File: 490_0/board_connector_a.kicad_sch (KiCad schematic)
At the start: 7 parts, among them J21 DF40HC(3.0)-100DS-0.4V(58), J22 DF40HC(3.0)-100DS-0.4V(58), J23 TS-102-G-A

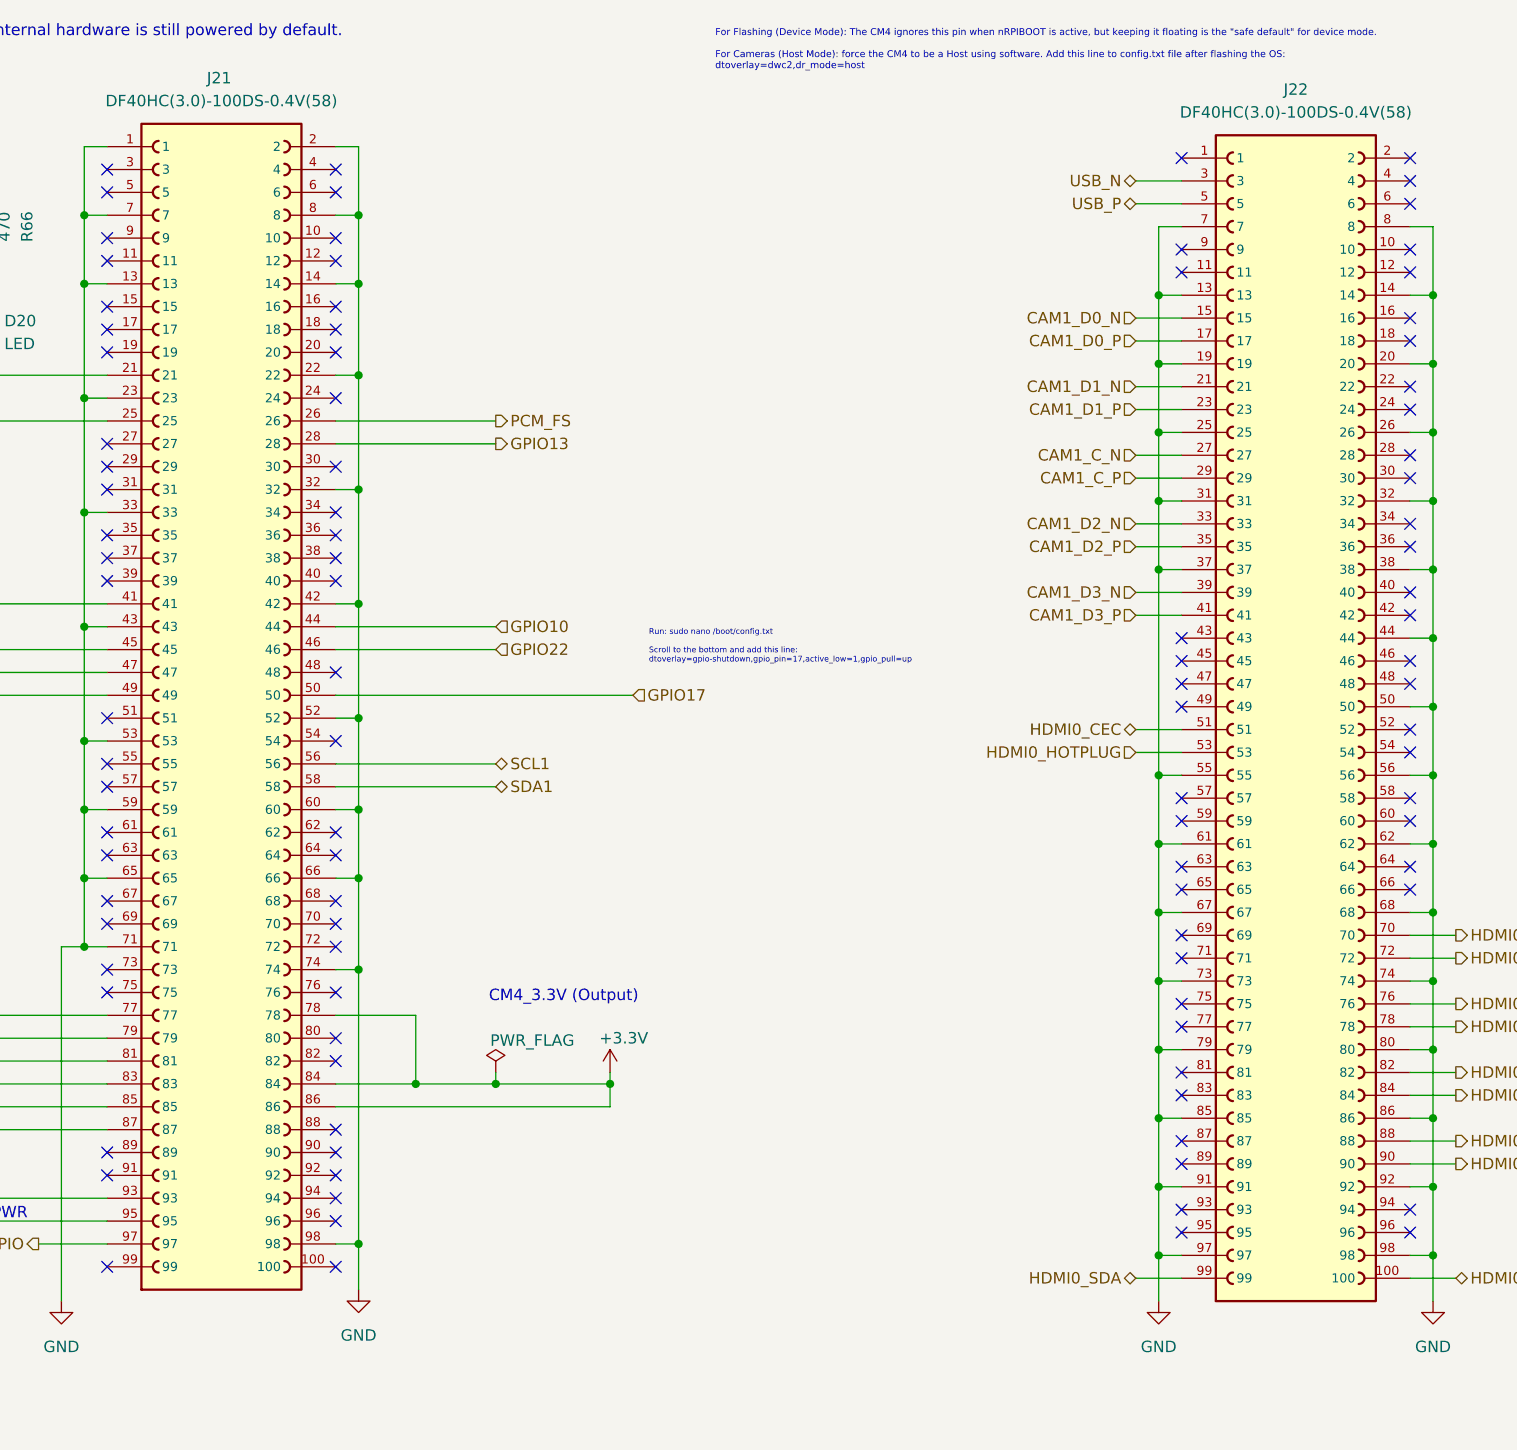
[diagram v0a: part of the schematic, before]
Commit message: Changed buck converter chip
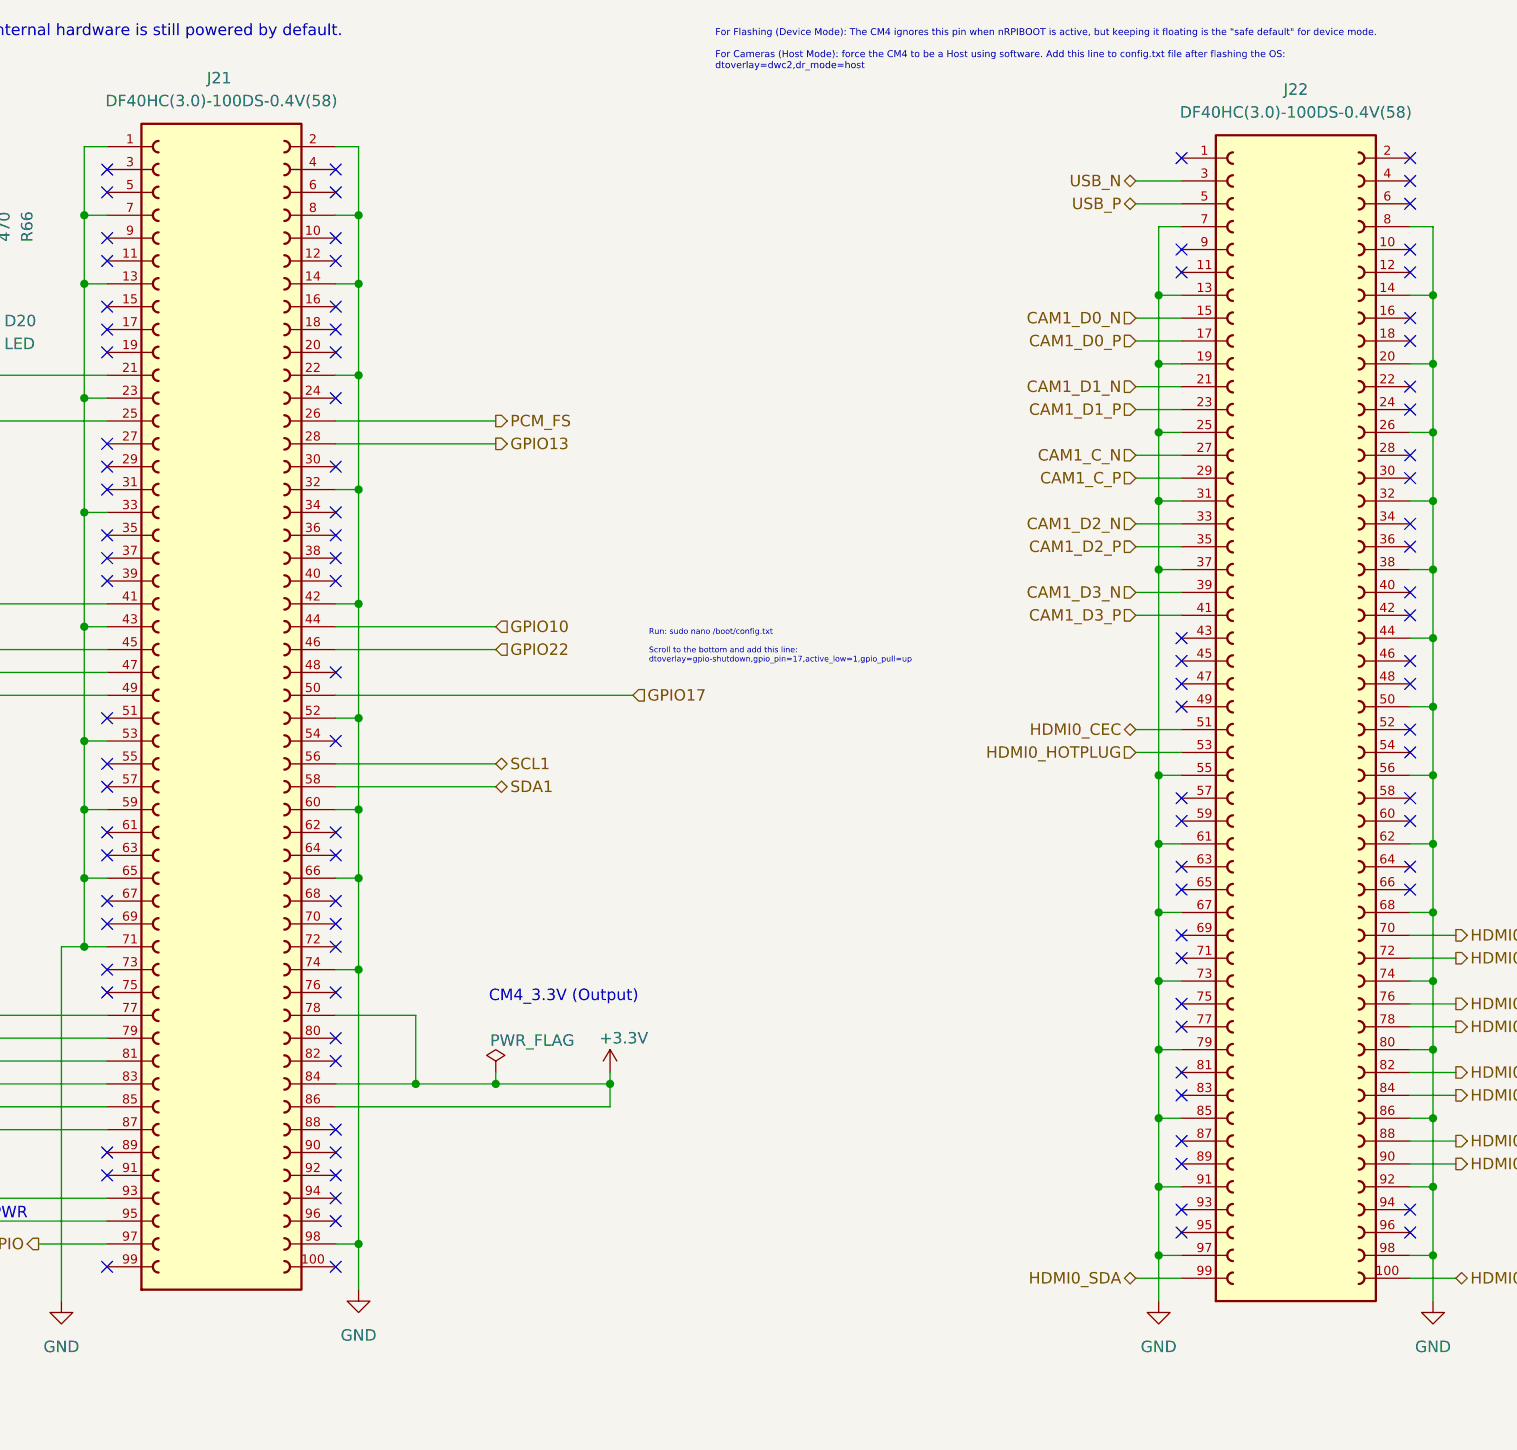
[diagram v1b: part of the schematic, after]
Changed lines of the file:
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@@
 	)
 	(symbol
+		(lib_name "DF40C-100DS-0.4V_51__1")
 		(lib_id "capstone_parts:DF40C-100DS-0.4V_51_")
 		(at 111.76 87.63 0)

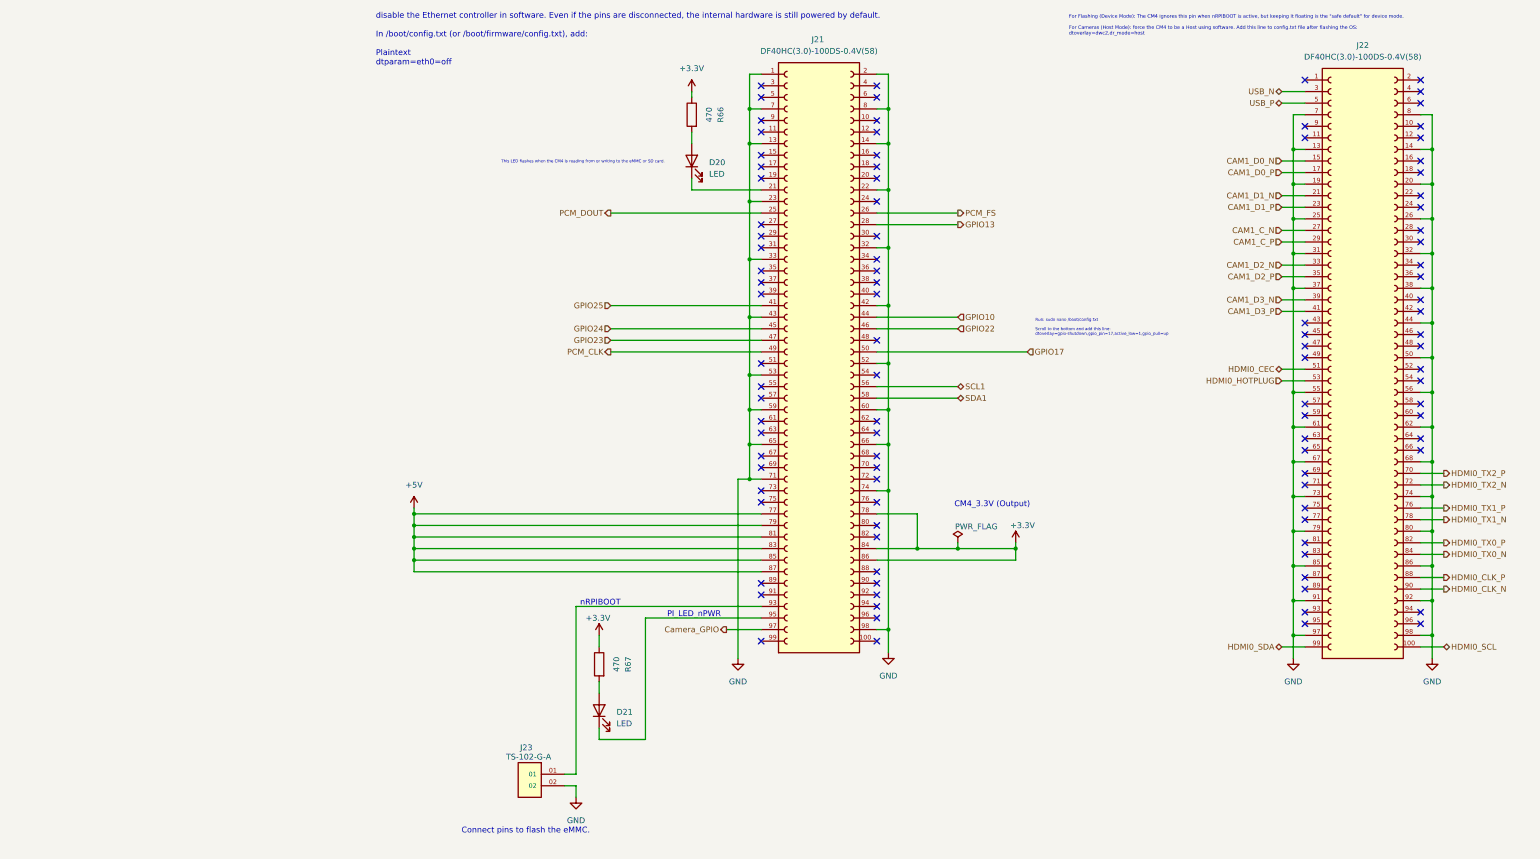
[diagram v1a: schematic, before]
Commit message: Implemented Dmitry comments
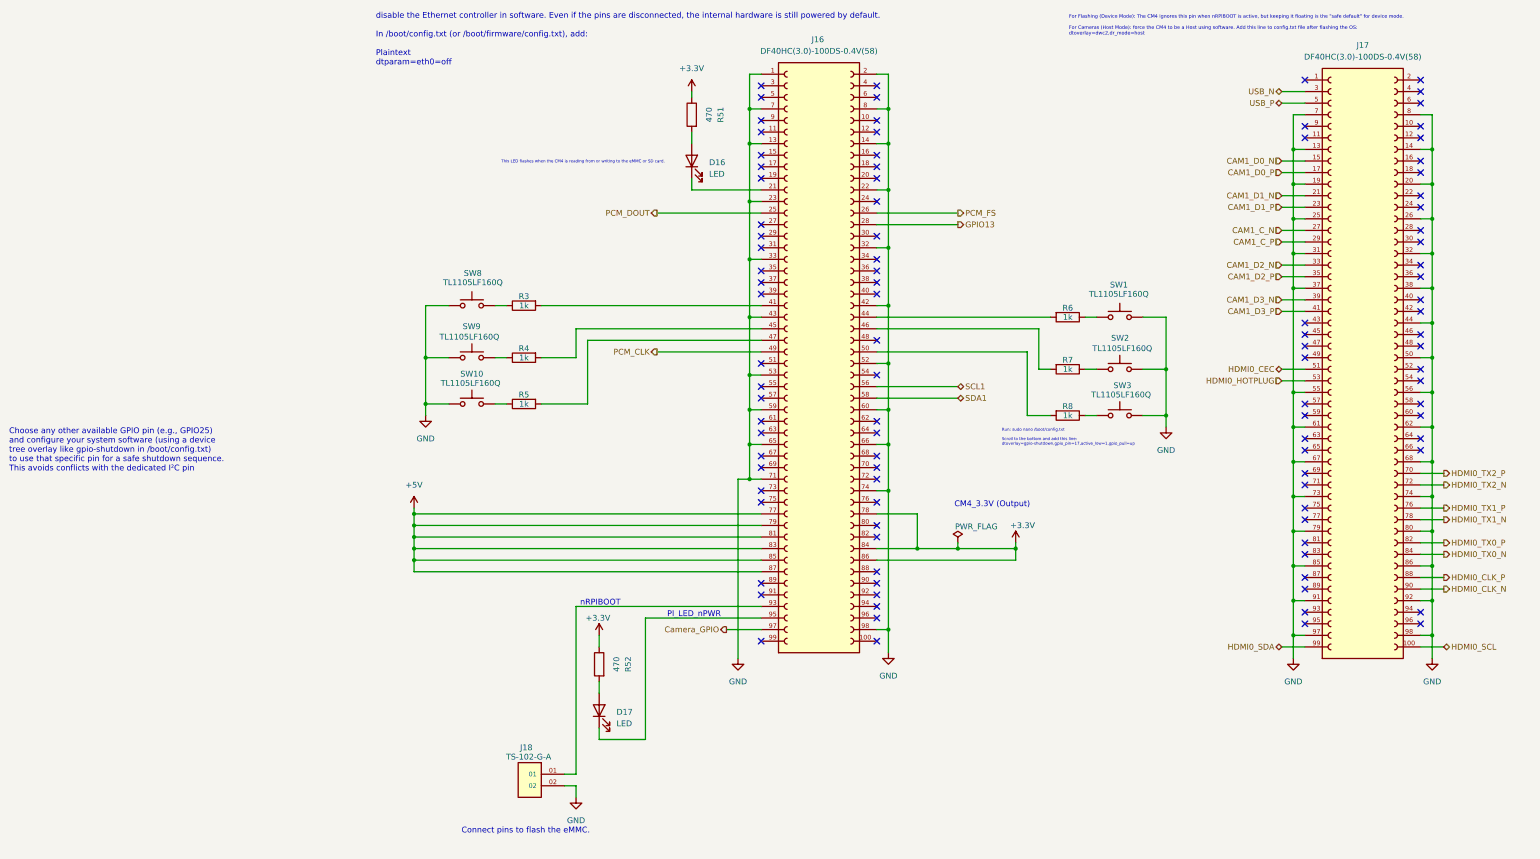
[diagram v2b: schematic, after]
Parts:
- added R3, R4, R5, R6, R7, R8: 1k, symbol Device:R
- added SW1, SW10, SW2, SW3, SW8, SW9: TL1105LF160Q, symbol Switch:SW_Push
- renumbered D20 to D16, D21 to D17, J21 to J16, J22 to J17, J23 to J18, R66 to R51, R67 to R52
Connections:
- net GND: now also SW1.1, SW10.1, SW2.1, SW3.1, SW8.1, SW9.1
- net GPIO10: no longer names the net of J16.44
- net GPIO10: now also R6.2
- net GPIO17: no longer names the net of J16.50
- net GPIO17: now also R8.2
- net GPIO22: no longer names the net of J16.46
- net GPIO22: now also R7.2
- net GPIO23: no longer names the net of J16.47
- net GPIO23: now also R5.2
- net GPIO24: no longer names the net of J16.45
- net GPIO24: now also R4.2
- net GPIO25: no longer names the net of J16.41
- net GPIO25: now also R3.2
- new net: R7.1, SW2.2
- new net: R5.1, SW10.2
- new net: R6.1, SW1.2
- new net: R4.1, SW9.2
- new net: R3.1, SW8.2
- new net: R8.1, SW3.2
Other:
- note added: "Choose any other available GPIO pin (e.g., GPIO25) and configure your system software (using a device tree overlay like gpio-shutdown in /boot/config.txt) to use that specific pin for a safe shutdown sequence. This avoids conflicts with the dedicated I²C pin"

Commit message: Final Fixes
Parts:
- renumbered R51 to R37, R3 to R38, R6 to R39, R4 to R40, R7 to R41, R5 to R42, R8 to R43, R52 to R44, SW8 to SW2, SW1 to SW3, SW9 to SW4, SW2 to SW5, SW10 to SW6, SW3 to SW7
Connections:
- net CAM1_D2_N: no longer names the net of J17.33
- net CAM1_D2_P: no longer names the net of J17.35
- net CAM1_D3_N: no longer names the net of J17.39
- net CAM1_D3_P: no longer names the net of J17.41
- no-connect marks 100 -> 104

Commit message: Implemented Dmitry recommendations
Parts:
- removed R38, R39, R40, R41, R42, R43: 1k, symbol Device:R
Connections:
- net at SW5.2: now also J16.46
- net at J16.41: now also SW2.2
- net at J16.44: now also SW3.2
- net at J16.45: now also SW4.2
- net at J16.47: now also SW6.2
- net at J16.50: now also SW7.2

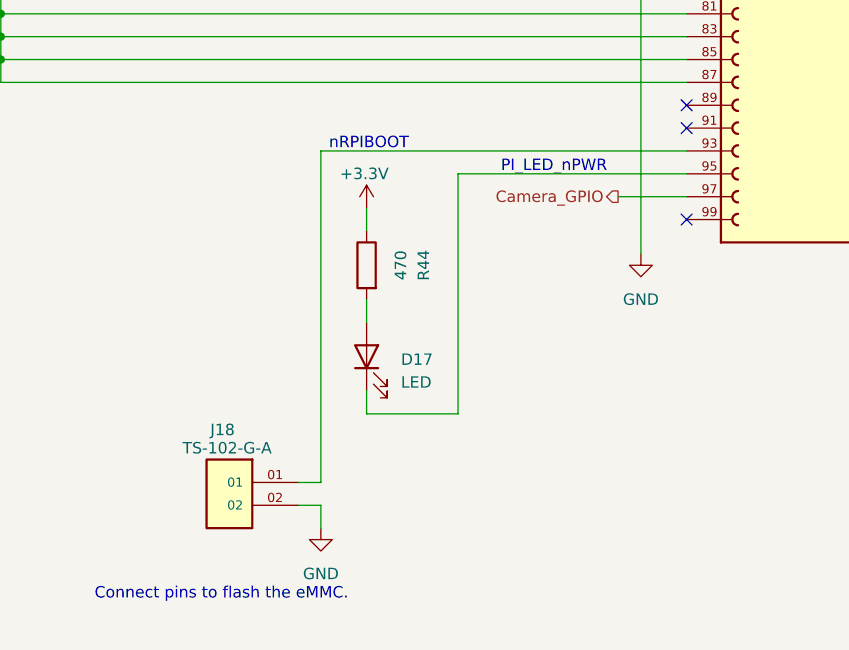
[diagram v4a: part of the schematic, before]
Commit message: Implemented suggestions
notes on schematics:
Overall: Schematics needs to be improved, more compact and cleaner
=========================
I) on root page (page 1):
overall: needs a bit of clean up of the diagram

1. the diagram shows pcb3 and pcb1, but no pcb2, it is probably outdated and therefore might have errors in it, fix it to the latest version and rename things to reflect what it actually is. Also try to clean it up a bit
2. The PCB-3 seem to have the cameras directly connected to the usb hub, how will this be connected? with connectors? if so add them to the diagram, if it's with wires soldered directly to the pcb, try to make note of it for clarity
4. for some reason your TOF is above PCB-3 but is only connected to PCB1, will the TOF be on the glasses, or will you be moving this to the main board? maybe have TOF on the chest for depth, and 2 cameras on glasses for vision, it will also reduce length of cable, which is ideal, i don't think it will work if you run it from the glasses to pcb1 though.
I know, this is a problem, we discussed the chest thing, the problem is the length of the cable but also the haptic feedback is weird if they turn their head.
5. Rename PCB1/PCB3 to PCB1 (chest) PCB3 (glasses) for clarity. Also i don't think (mayeb i'm wrong) that the 5 conected buttons should be on a bus, a bus implies that multiple devices communicate on the same single line. You're using individual lines for each to individual gpio, no?

=========================
II) on PCB-3 usb 2.0 bridge page (page 10)
overall: check datasheet and make sure you've done the connection right and values are selected properly, with the chip data lines properly pulled up/down whether externally or internally. This is important

1. C3/C11 are the input capacitors to U2/u3 TPS553DBVR, datasheet says 100nF, you used 10uF, why? stick to 100nF
2. you seem to have implemented one of /Uthe typical application circuit, look at the others. You have on page 21 of datasheet an auto-retry wi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
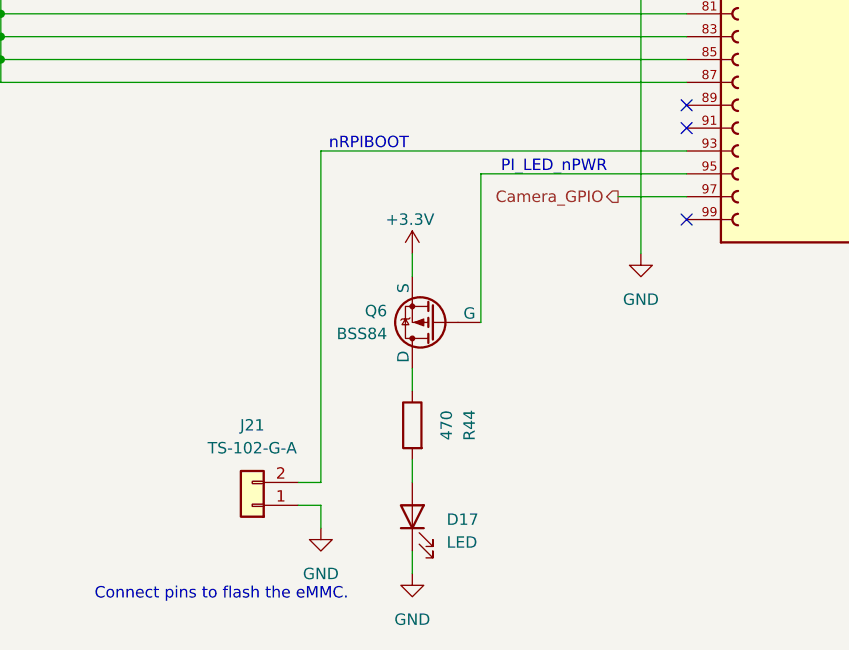
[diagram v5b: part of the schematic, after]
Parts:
- removed J18: TS-102-G-A, TS-102-G-A:SAMTEC_TS-102-G-A, symbol capstone_parts:TS-102-G-A
- added J21: TS-102-G-A, 4ms_Connector:Pins_1x02_2.54mm_TH, symbol PCM_4ms_Connector:Conn_01x02
- added Q6: BSS84, symbol Simulation_SPICE:PMOS
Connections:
- net +3.3V: now also Q6.3 (S); no longer R44.1
- net GND: now also D17.1 (K), J21.1 (Pin_1)
- net at J16.93: now also J21.2 (Pin_2)
- net at J16.95: now also Q6.2 (G); no longer D17.1 (K)
- new net: Q6.1 (D), R44.1
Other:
- moved on the sheet: D17, R44

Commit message: Footprint Update
1st half of footprints updated
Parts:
- D16: footprint (none) -> LED_SMD:LED_0805_2012Metric
- D17: footprint PCM_Diode_SMD_AKL:D_SOD-123F -> LED_SMD:LED_0805_2012Metric
- J16, J17: footprint DF40C-100DS-0.4V_51_:HIROSE_DF40C-100DS-0.4V_51_ -> *CapStone*:HIROSE_DF40C-100DS-0.4V_51_
- J21: footprint 4ms_Connector:Pins_1x02_2.54mm_TH -> *CapStone*:CON2_1X2_TU_HTS_SAI
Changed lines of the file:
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@@
 			)
 		)
-		(property "Footprint" "DF40C-100DS-0.4V_51_:HIROSE_DF40C-100DS-0.4V_51_"
+		(property "Footprint" "*CapStone*:HIROSE_DF40C-100DS-0.4V_51_"
 			(at 111.76 87.63 0)
 			(effects
@@
 			)
 		)
-		(property "Footprint" ""
+		(property "Footprint" "LED_SMD:LED_0805_2012Metric"
 			(at 83.82 45.72 0)
 			(effects
@@
 			)
 		)
-		(property "Footprint" "DF40C-100DS-0.4V_51_:HIROSE_DF40C-100DS-0.4V_51_"
+		(property "Footprint" "*CapStone*:HIROSE_DF40C-100DS-0.4V_51_"
 			(at 231.14 88.9 0)
 			(effects
@@
 			)
 		)
-		(property "Footprint" "PCM_Diode_SMD_AKL:D_SOD-123F"
+		(property "Footprint" "LED_SMD:LED_0805_2012Metric"
 			(at 68.58 184.15 0)
 			(effects
@@
 			)
 		)
-		(property "Footprint" "4ms_Connector:Pins_1x02_2.54mm_TH"
+		(property "Footprint" "*CapStone*:CON2_1X2_TU_HTS_SAI"
 			(at 51.435 187.325 0)
 			(effects
